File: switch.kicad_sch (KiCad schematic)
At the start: 3 parts

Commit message: uses SPI2 instead of SPI in name. Refs: #1
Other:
- sheet switch_gpios ports: added SPI2_STM_SWITCH{MOSI,MISO,nCS,CLK}; removed SPI_STM_SWITCH{MOSI,MISO,nCS,CLK}
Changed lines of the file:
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@@
 			)
 		)
-		(pin "SPI_STM_SWITCH{MOSI,MISO,nCS,CLK}" bidirectional
+		(pin "SPI2_STM_SWITCH{MOSI,MISO,nCS,CLK}" bidirectional
 			(at 102.87 92.71 90)
 			(effects

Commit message: fixes incorrect SPI2 naming on switch sheets. Refs: #1
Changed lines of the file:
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@@
 		)
 	)
-	(hierarchical_label "SPI_STM_SWITCH{MOSI,MISO,nCS,CLK}"
+	(hierarchical_label "SPI2_STM_SWITCH{MOSI,MISO,nCS,CLK}"
 		(shape bidirectional)
 		(at 92.71 57.15 180)

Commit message: removes 25M CLK input for switch. Refs: #1
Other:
- sheet switch_power ports: added none; removed 25M_CLKIN
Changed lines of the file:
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@@
 	(wire
 		(pts
-			(xy 189.23 134.62) (xy 213.36 134.62)
-		)
-		(stroke
-			(width 0)
-			(type default)
-		)
-	)
-	(wire
-		(pts
 			(xy 189.23 104.14) (xy 213.36 104.14)
-		)
-		(stroke
-			(width 0)
-			(type default)
-		)
-	)
-	(wire
-		(pts
-			(xy 72.39 26.67) (xy 96.52 26.67)
 		)
 		(stroke
@@
 			)
 			(justify left bottom)
-		)
-	)
-	(label "CLK-25M_OSC"
-		(at 189.23 134.62 0)
-		(effects
-			(font
-				(size 1.27 1.27)
-			)
-			(justify left bottom)
-		)
-	)
-	(label "CLK-25M_OSC"
-		(at 96.52 26.67 180)
-		(effects
-			(font
-				(size 1.27 1.27)
-			)
-			(justify right bottom)
 		)
 	)
@@
 		(shape bidirectional)
 		(at 92.71 57.15 180)
-		(effects
-			(font
-				(size 1.27 1.27)
-			)
-			(justify right)
-		)
-	)
-	(hierarchical_label "CLK-25M_OSC"
-		(shape input)
-		(at 72.39 26.67 180)
 		(effects
 			(font
@@
 			(effects
 				(font
-					(size 1.27 1.27)
-				)
-				(justify left)
-			)
-		)
-		(pin "25M_CLKIN" input
-			(at 213.36 134.62 180)
-			(effects
-				(font

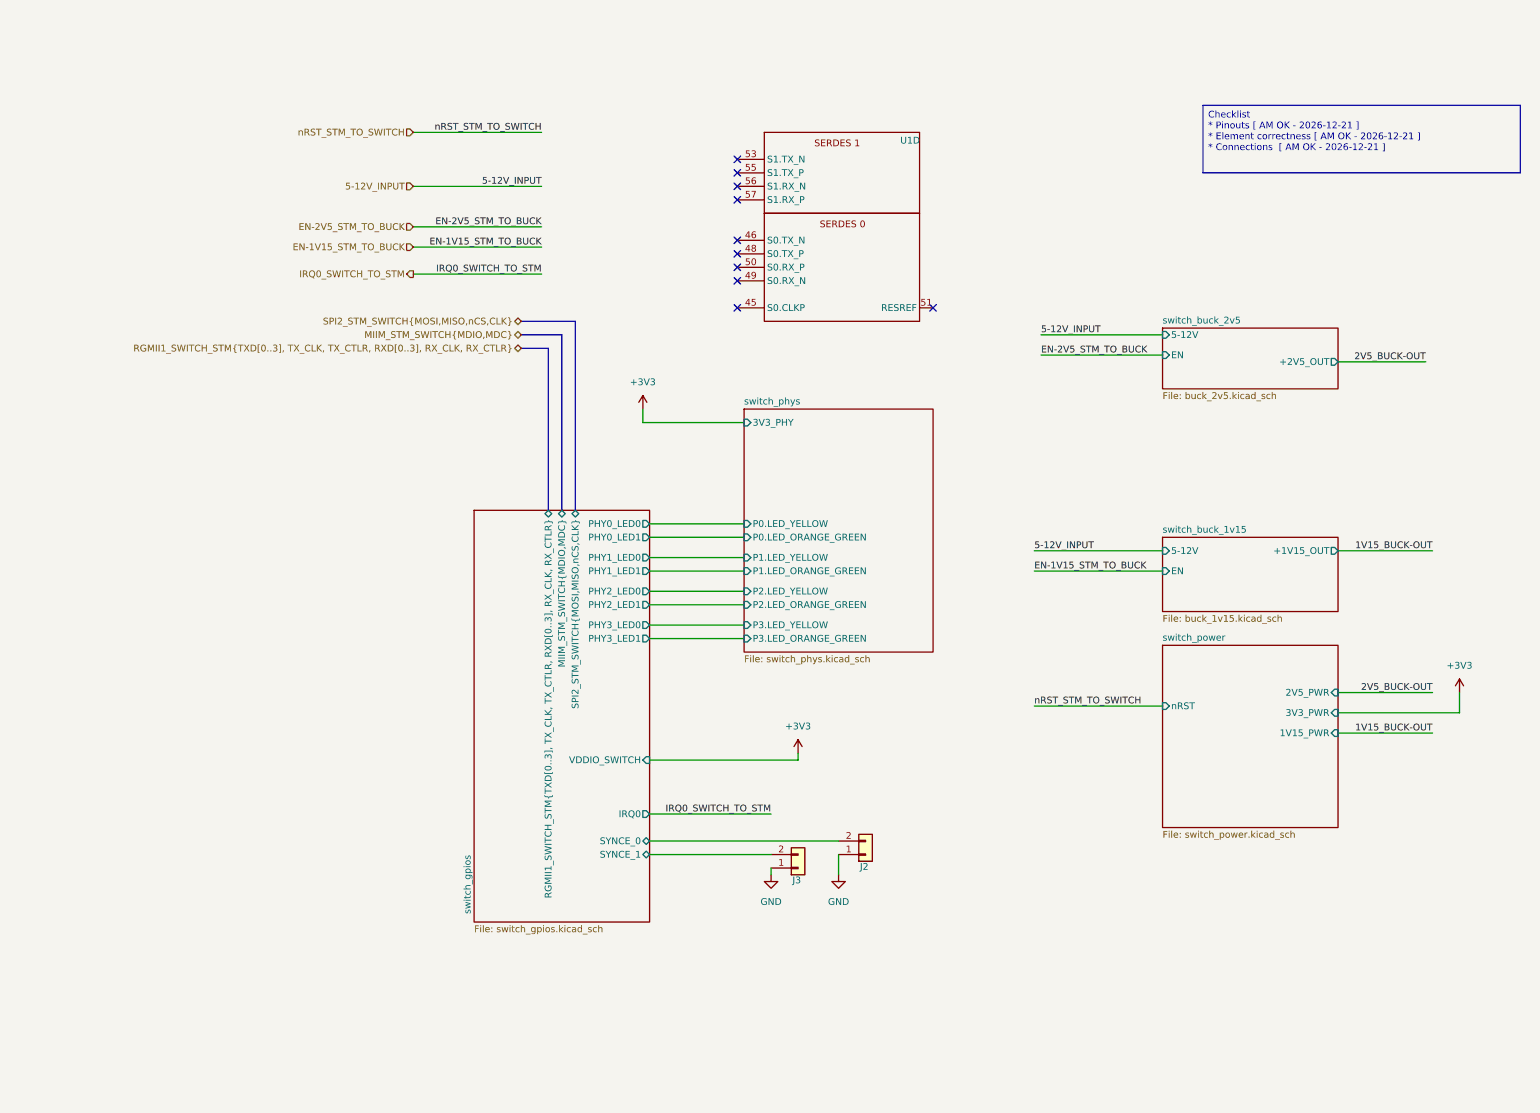
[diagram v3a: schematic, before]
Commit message: RGMII1 bus uses Microchip names. Refs: #1
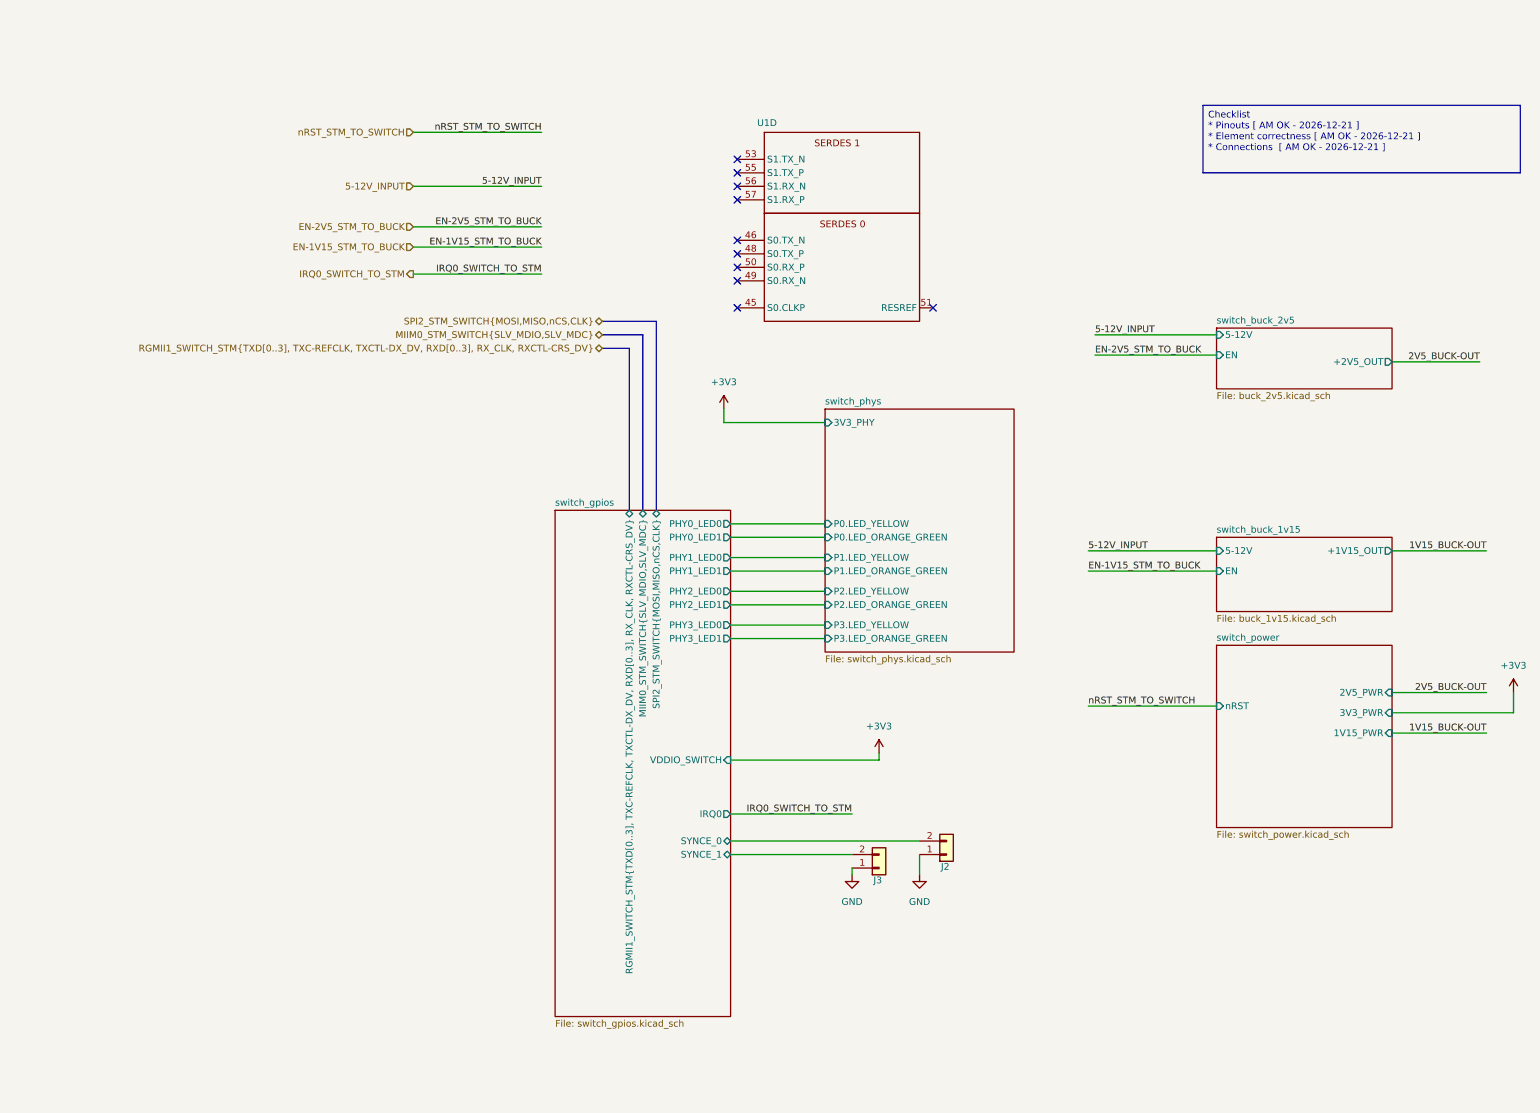
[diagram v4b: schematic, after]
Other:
- sheet switch_gpios ports: added MIIM0_STM_SWITCH{SLV_MDIO,SLV_MDC}, RGMII1_SWITCH_STM{TXD[0..3], TXC-REFCLK, TXCTL-DX_DV, RXD[0..3], RX_CLK, RXCTL-CRS_DV}; removed MIIM_STM_SWITCH{MDIO,MDC}, RGMII1_SWITCH_STM{TXD[0..3], TX_CLK, TX_CTLR, RXD[0..3], RX_CLK, RX_CTLR}
- moved on the sheet: J2, J3

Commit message: updates component details for ordering. Refs: #1
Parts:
- J2, J3: value ~ -> 02x01_2.54mm_Header; Digikey (none) -> A26543-ND; LCSC (none) -> C5383111; Mouser (none) -> 571-872242
- U1: value ~ -> LAN96455F-I/8MW; Digikey (none) -> 150-LAN96455F-I/8MW-ND; Mouser (none) -> 579-LAN96455FI8MW; manf# LAN96455F-I/8MW -> (none)
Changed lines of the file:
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@@
 			)
 		)
-		(property "Value" "~"
+		(property "Value" "02x01_2.54mm_Header"
 			(at 172.72 156.21 0)
 			(effects
@@
 		)
 		(property "Description" ""
+			(at 172.72 156.21 0)
+			(effects
+				(font
+					(size 1.27 1.27)
+				)
+				(hide yes)
+			)
+		)
+		(property "Mouser" "571-872242"
+			(at 172.72 156.21 0)
+			(effects
+				(font
+					(size 1.27 1.27)
+				)
+				(hide yes)
+			)
+		)
+		(property "Digikey" "A26543-ND"
+			(at 172.72 156.21 0)
+			(effects
+				(font
+					(size 1.27 1.27)
+				)
+				(hide yes)
+			)
+		)
+		(property "LCSC" "C5383111"
 			(at 172.72 156.21 0)
 			(effects
@@
 			)
 		)
-		(property "Value" "~"
+		(property "Value" "02x01_2.54mm_Header"
 			(at 160.02 158.75 0)
 			(effects
@@
 		)
 		(property "Description" ""
+			(at 160.02 158.75 0)
+			(effects
+				(font
+					(size 1.27 1.27)
+				)
+				(hide yes)
+			)
+		)
+		(property "Mouser" "571-872242"
+			(at 160.02 158.75 0)
+			(effects
+				(font
+					(size 1.27 1.27)
+				)
+				(hide yes)
+			)
+		)
+		(property "Digikey" "A26543-ND"
+			(at 160.02 158.75 0)
+			(effects
+				(font
+					(size 1.27 1.27)
+				)
+				(hide yes)
+			)
+		)
+		(property "LCSC" "C5383111"
 			(at 160.02 158.75 0)
 			(effects
@@
 			)
 		)
-		(property "Value" "~"
+		(property "Value" "LAN96455F-I/8MW"
 			(at 138.43 38.1 0)
 			(effects
@@
 			)
 		)
-		(property "manf#" "LAN96455F-I/8MW"
-			(at 153.67 12.192 0)
-			(effects
-				(font
+		(property "Mouser" "579-LAN96455FI8MW"
+			(at 138.43 21.59 0)
+			(effects
+				(font
+					(size 1.27 1.27)
+				)
+				(hide yes)
+			)
+		)
+		(property "Digikey" "150-LAN96455F-I/8MW-ND"
+			(at 138.43 21.59 0)
+			(effects
+				(font
+					(size 1.27 1.27)
+				)
+				(hide yes)
+			)
+		)
+		(property "LCSC" ""
+			(at 138.43 21.59 0)
+			(effects
+				(font

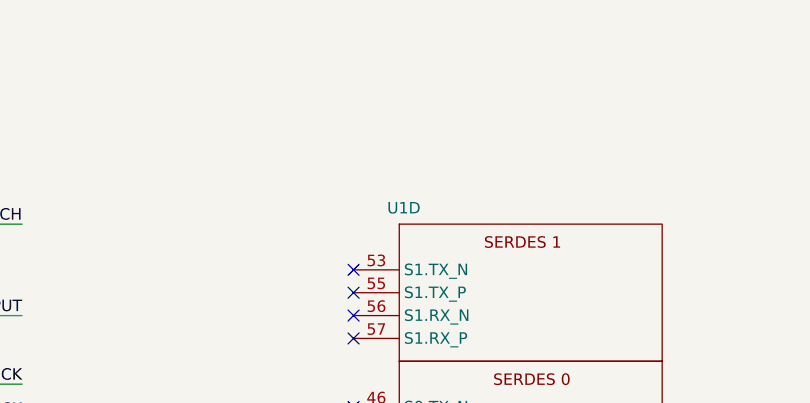
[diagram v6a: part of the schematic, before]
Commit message: initial commit for automatic current consumption calculation. Refs: #9
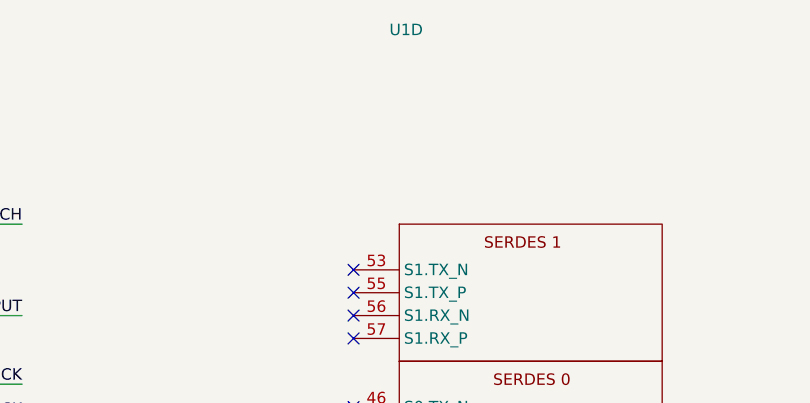
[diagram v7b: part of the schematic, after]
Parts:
- U1: I_DD_1V15_max_A (none) -> 0.935; I_DD_AH25_2V5_max_A (none) -> 0.475; I_DD_AH33_3V3_max_A (none) -> 0.505; I_DD_ALSx_1V15_max_A (none) -> 0.025; I_DD_AL_1V15_max_A (none) -> 0.400; I_DD_IO25_2V5_max_A (none) -> 0.045; I_DD_IO33_3V3_max_A (none) -> 0.075; I_DD_IOD (none) -> 0.005
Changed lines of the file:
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@@
 		(dnp no)
 		(property "Reference" "U1"
-			(at 138.938 19.812 0)
+			(at 139.192 0 0)
 			(effects
 				(font
@@
 			(at 138.43 21.59 0)
 			(effects
+				(font
+					(size 1.27 1.27)
+				)
+				(hide yes)
+			)
+		)
+		(property "I_DD_1V15_max_A" "0.935"
+			(at 138.43 21.59 0)
+			(effects
+				(font
+					(size 1.27 1.27)
+				)
+				(hide yes)
+			)
+		)
+		(property "I_DD_AL_1V15_max_A" "0.400"
+			(at 138.43 21.59 0)
+			(effects
+				(font
+					(size 1.27 1.27)
+				)
+				(hide yes)
+			)
+		)
+		(property "I_DD_ALSx_1V15_max_A" "0.025"
+			(at 138.43 21.59 0)
+			(effects
+				(font
+					(size 1.27 1.27)
+				)
+				(hide yes)
+			)
+		)
+		(property "I_DD_AH25_2V5_max_A" "0.475"
+			(at 138.43 21.59 0)
+			(effects
+				(font
+					(size 1.27 1.27)
+				)
+				(hide yes)
+			)
+		)
+		(property "I_DD_AH33_3V3_max_A" "0.505"
+			(at 138.43 21.59 0)
+			(effects
+				(font
+					(size 1.27 1.27)
+				)
+				(hide yes)
+			)
+		)
+		(property "I_DD_IO25_2V5_max_A" "0.045"
+			(at 138.43 21.59 0)
+			(effects
+				(font
+					(size 1.27 1.27)
+				)
+				(hide yes)
+			)
+		)
+		(property "I_DD_IO33_3V3_max_A" "0.075"
+			(at 138.43 21.59 0)
+			(effects
+				(font
+					(size 1.27 1.27)
+				)
+				(hide yes)
+			)
+		)
+		(property "I_DD_IOD" "0.005"
+			(at 138.43 21.59 0)
+			(effects
